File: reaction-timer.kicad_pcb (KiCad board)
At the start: 2 copper layers, 48 x 80 mm, 38 parts, among them IC1 4026, IC2 4026, IC3 4026, IC5 NE555P, IC6 NE555P, IC7 NE555P

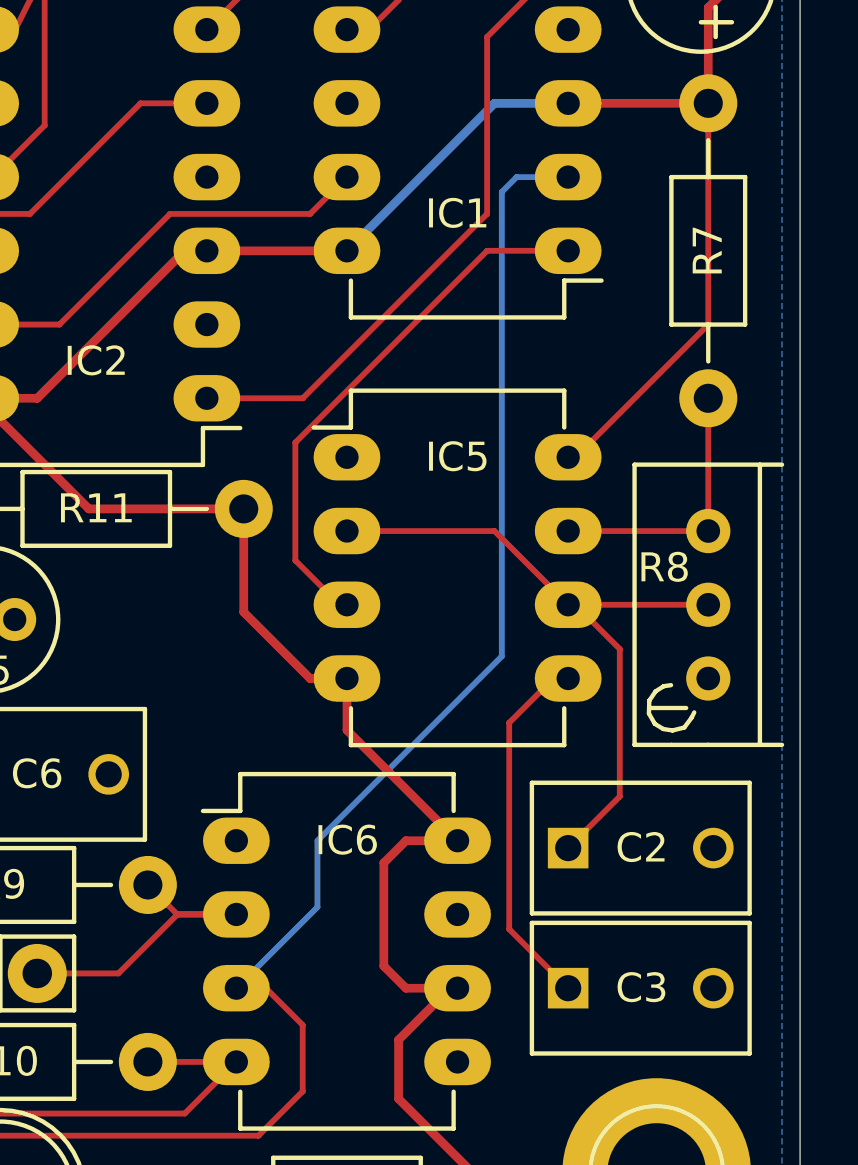
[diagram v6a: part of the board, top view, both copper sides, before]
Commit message: Move bottom layer trace to improve ground fill
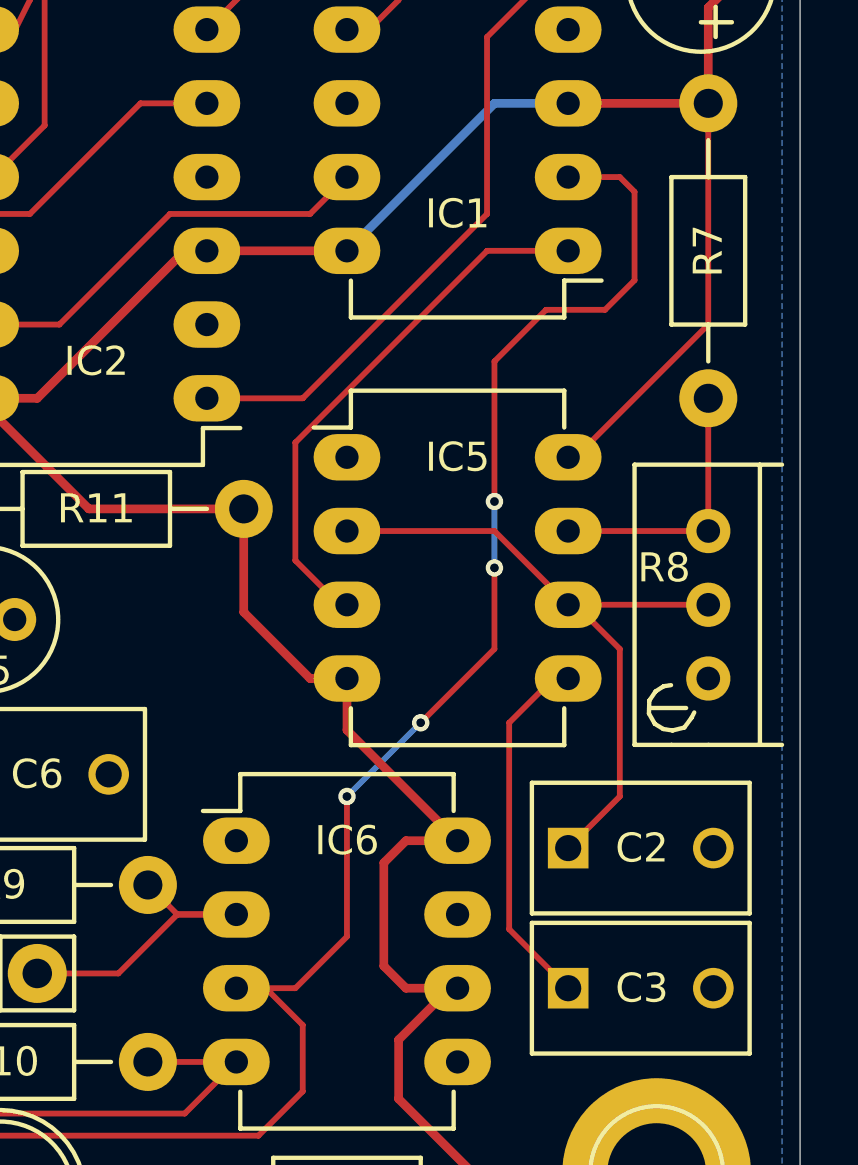
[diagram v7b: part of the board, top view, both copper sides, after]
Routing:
- net Net-(IC1-Pad2): track 52.7 -> 57.0 mm, vias 0 -> 4
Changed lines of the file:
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@@
     (thickness 1.6)
     (drawings 8)
-    (tracks 320)
+    (tracks 332)
     (zones 0)
     (modules 38)
@@
   (segment (start 89.408 116.332) (end 87.884 114.808) (width 0.2) (layer F.Cu) (net 40))
   (segment (start 89.662 116.332) (end 89.408 116.332) (width 0.2) (layer F.Cu) (net 40))
-  (segment (start 97.282 101.6) (end 95.504 101.6) (width 0.2) (layer B.Cu) (net 41))
-  (segment (start 88.646 126.746) (end 85.852 129.54) (width 0.2) (layer B.Cu) (net 41))
-  (segment (start 88.646 124.46) (end 88.646 126.746) (width 0.2) (layer B.Cu) (net 41))
-  (segment (start 94.996 118.11) (end 88.646 124.46) (width 0.2) (layer B.Cu) (net 41))
-  (segment (start 94.996 102.108) (end 94.996 118.11) (width 0.2) (layer B.Cu) (net 41))
-  (segment (start 95.504 101.6) (end 94.996 102.108) (width 0.2) (layer B.Cu) (net 41))
+  (segment (start 85.852 129.54) (end 87.884 129.54) (width 0.2) (layer F.Cu) (net 41))
+  (segment (start 99.06 101.6) (end 97.282 101.6) (width 0.2) (layer F.Cu) (net 41))
+  (segment (start 99.568 102.108) (end 99.06 101.6) (width 0.2) (layer F.Cu) (net 41))
+  (segment (start 99.568 105.156) (end 99.568 102.108) (width 0.2) (layer F.Cu) (net 41))
+  (segment (start 98.552 106.172) (end 99.568 105.156) (width 0.2) (layer F.Cu) (net 41))
+  (segment (start 96.52 106.172) (end 98.552 106.172) (width 0.2) (layer F.Cu) (net 41))
+  (segment (start 94.742 107.95) (end 96.52 106.172) (width 0.2) (layer F.Cu) (net 41))
+  (segment (start 94.742 112.776) (end 94.742 107.95) (width 0.2) (layer F.Cu) (net 41))
+  (via (at 94.742 112.776) (size 0.6) (layers F.Cu B.Cu) (net 41))
+  (segment (start 94.742 115.062) (end 94.742 112.776) (width 0.2) (layer B.Cu) (net 41))
+  (via (at 94.742 115.062) (size 0.6) (layers F.Cu B.Cu) (net 41))
+  (segment (start 94.742 117.856) (end 94.742 115.062) (width 0.2) (layer F.Cu) (net 41))
+  (segment (start 92.202 120.396) (end 94.742 117.856) (width 0.2) (layer F.Cu) (net 41))
+  (via (at 92.202 120.396) (size 0.6) (layers F.Cu B.Cu) (net 41))
+  (segment (start 89.662 122.936) (end 92.202 120.396) (width 0.2) (layer B.Cu) (net 41))
+  (via (at 89.662 122.936) (size 0.6) (layers F.Cu B.Cu) (net 41))
+  (segment (start 89.662 127.762) (end 89.662 122.936) (width 0.2) (layer F.Cu) (net 41))
+  (segment (start 87.884 129.54) (end 89.662 127.762) (width 0.2) (layer F.Cu) (net 41))
   (segment (start 86.868 129.54) (end 85.852 129.54) (width 0.2) (layer F.Cu) (net 41))
   (segment (start 76.45266 135.38334) (end 77.216 134.62) (width 0.2) (layer F.Cu) (net 41))
